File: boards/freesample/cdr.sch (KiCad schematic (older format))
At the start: 76 parts, among them J6 XILINX_JTAG, U13 SIP32408, U5 TLK10232, U6 LMK61PD0A2

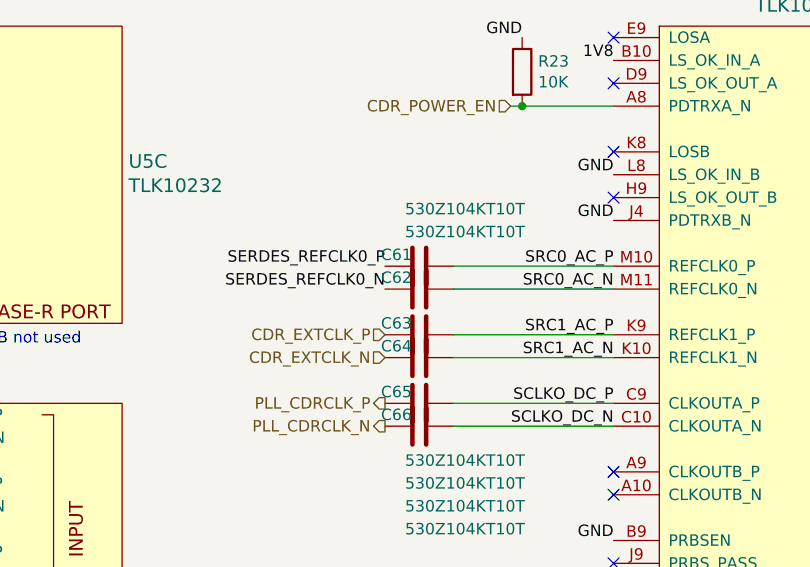
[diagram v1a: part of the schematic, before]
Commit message: Swapped clock inputs to TLK10232 to reduce via count. Began PLL layout.
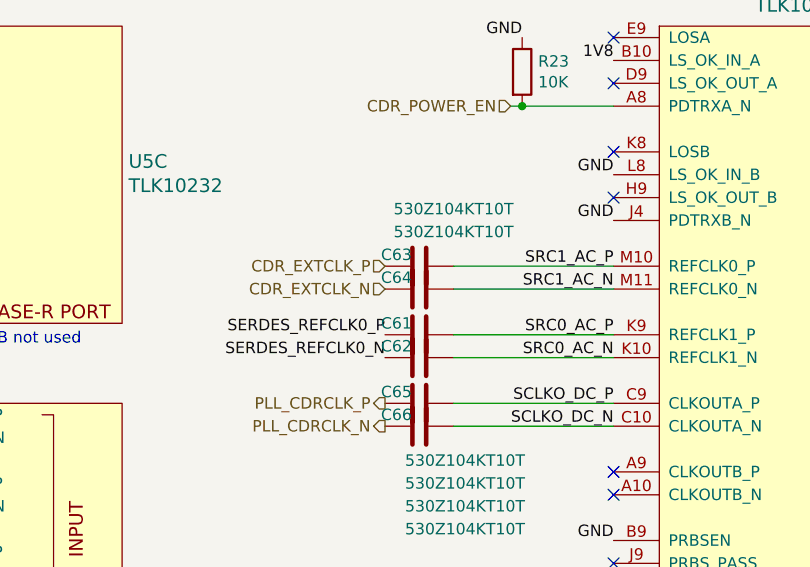
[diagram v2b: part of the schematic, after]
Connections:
- net SRC0_AC_N: now also U5.K10 (REFCLK1_N); no longer U5.M11 (REFCLK0_N)
- net SRC0_AC_P: now also U5.K9 (REFCLK1_P); no longer U5.M10 (REFCLK0_P)
- net SRC1_AC_N: now also U5.M11 (REFCLK0_N); no longer U5.K10 (REFCLK1_N)
- net SRC1_AC_P: now also U5.M10 (REFCLK0_P); no longer U5.K9 (REFCLK1_P)
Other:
- moved on the sheet: C61, C62, C63, C64
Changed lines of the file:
@@
 Sheet 4 12
 Title "FREESAMPLE Oscilloscope"
-Date "2019-03-20"
+Date "2019-03-21"
 Rev "0.1"
 Comp "Andrew D. Zonenberg / Antikernel Labs"
@@
 NoConn ~ 5300 1550
 NoConn ~ 5300 1350
-Text HLabel 4300 2250 0    50   Input ~ 0
-CDR_EXTCLK_N
 Text HLabel 4300 2450 0    50   Output ~ 0
 PLL_CDRCLK_P
@@
 Text Label 5300 950  2    50   ~ 0
 1V8
-Text Label 4300 1850 2    50   ~ 0
+Text Label 4300 2150 2    50   ~ 0
 SERDES_REFCLK0_P
-Text Label 4300 1950 2    50   ~ 0
+Text Label 4300 2250 2    50   ~ 0
 SERDES_REFCLK0_N
 $Comp
 L device:C C61
 U 1 1 5C776A8A
-P 4450 1850
-F 0 "C61" V 4400 1750 50  0000 C CNN
-F 1 "530Z104KT10T" V 4200 2050 50  0000 C CNN
-F 2 "azonenberg_pcb:EIA_0201_CAP_NOSILK" H 4488 1700 50  0001 C CNN
-F 3 "" H 4450 1850 50  0001 C CNN
-	1    4450 1850
-	0    1    1    0
-$EndComp
-$Comp
-L device:C C62
-U 1 1 5C777E42
-P 4450 1950
-F 0 "C62" V 4400 1850 50  0000 C CNN
-F 1 "530Z104KT10T" V 4200 2150 50  0000 C CNN
-F 2 "azonenberg_pcb:EIA_0201_CAP_NOSILK" H 4488 1800 50  0001 C CNN
-F 3 "" H 4450 1950 50  0001 C CNN
-	1    4450 1950
-	0    1    1    0
-$EndComp
-Text Label 5300 1850 2    50   ~ 0
-SRC0_AC_P
-Text Label 5300 1950 2    50   ~ 0
-SRC0_AC_N
-$Comp
-L device:C C63
-U 1 1 5C77E371
 P 4450 2150
-F 0 "C63" V 4400 2050 50  0000 C CNN
-F 1 "530Z104KT10T" V 5000 2350 50  0000 C CNN
+F 0 "C61" V 4400 2050 50  0000 C CNN
+F 1 "530Z104KT10T" V 4000 2300 50  0000 C CNN
 F 2 "azonenberg_pcb:EIA_0201_CAP_NOSILK" H 4488 2000 50  0001 C CNN
 F 3 "" H 4450 2150 50  0001 C CNN
@@
 $EndComp
 $Comp
-L device:C C64
-U 1 1 5C77E37B
+L device:C C62
+U 1 1 5C777E42
 P 4450 2250
-F 0 "C64" V 4400 2150 50  0000 C CNN
-F 1 "530Z104KT10T" V 5000 2450 50  0000 C CNN
+F 0 "C62" V 4400 2150 50  0000 C CNN
+F 1 "530Z104KT10T" V 3800 2400 50  0000 C CNN
 F 2 "azonenberg_pcb:EIA_0201_CAP_NOSILK" H 4488 2100 50  0001 C CNN
 F 3 "" H 4450 2250 50  0001 C CNN
@@
 $EndComp
 Text Label 5300 2150 2    50   ~ 0
-SRC1_AC_P
+SRC0_AC_P
 Text Label 5300 2250 2    50   ~ 0
-SRC1_AC_N
+SRC0_AC_N
 Wire Wire Line
 	4600 2250 5300 2250
 Wire Wire Line
 	4600 2150 5300 2150
-Wire Wire Line
-	4600 1950 5300 1950
-Wire Wire Line
-	4600 1850 5300 1850
 NoConn ~ 5300 2750
 NoConn ~ 5300 2850
@@
 Text Label 4900 850  2    50   ~ 0
 GND
-Text HLabel 4300 2150 0    50   Input ~ 0
+Text HLabel 4300 1850 0    50   Input ~ 0
 CDR_EXTCLK_P
+Wire Wire Line
+	4600 1850 5300 1850
+Wire Wire Line
+	4600 1950 5300 1950
+Text Label 5300 1950 2    50   ~ 0
+SRC1_AC_N
+Text Label 5300 1850 2    50   ~ 0
+SRC1_AC_P
+$Comp
+L device:C C64
+U 1 1 5C77E37B
+P 4450 1950
+F 0 "C64" V 4400 1850 50  0000 C CNN
+F 1 "530Z104KT10T" V 5300 2150 50  0000 C CNN
+F 2 "azonenberg_pcb:EIA_0201_CAP_NOSILK" H 4488 1800 50  0001 C CNN
+F 3 "" H 4450 1950 50  0001 C CNN
+	1    4450 1950
+	0    1    1    0
+$EndComp
+$Comp
+L device:C C63
+U 1 1 5C77E371
+P 4450 1850
+F 0 "C63" V 4400 1750 50  0000 C CNN
+F 1 "530Z104KT10T" V 5300 2050 50  0000 C CNN
+F 2 "azonenberg_pcb:EIA_0201_CAP_NOSILK" H 4488 1700 50  0001 C CNN
+F 3 "" H 4450 1850 50  0001 C CNN
+	1    4450 1850
+	0    1    1    0
+$EndComp
+Text HLabel 4300 1950 0    50   Input ~ 0
+CDR_EXTCLK_N
 $EndSCHEMATC
